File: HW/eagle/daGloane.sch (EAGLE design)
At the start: 62 parts, among them IC2 MCP1252-33X50, U1 STM32F10XTXU6

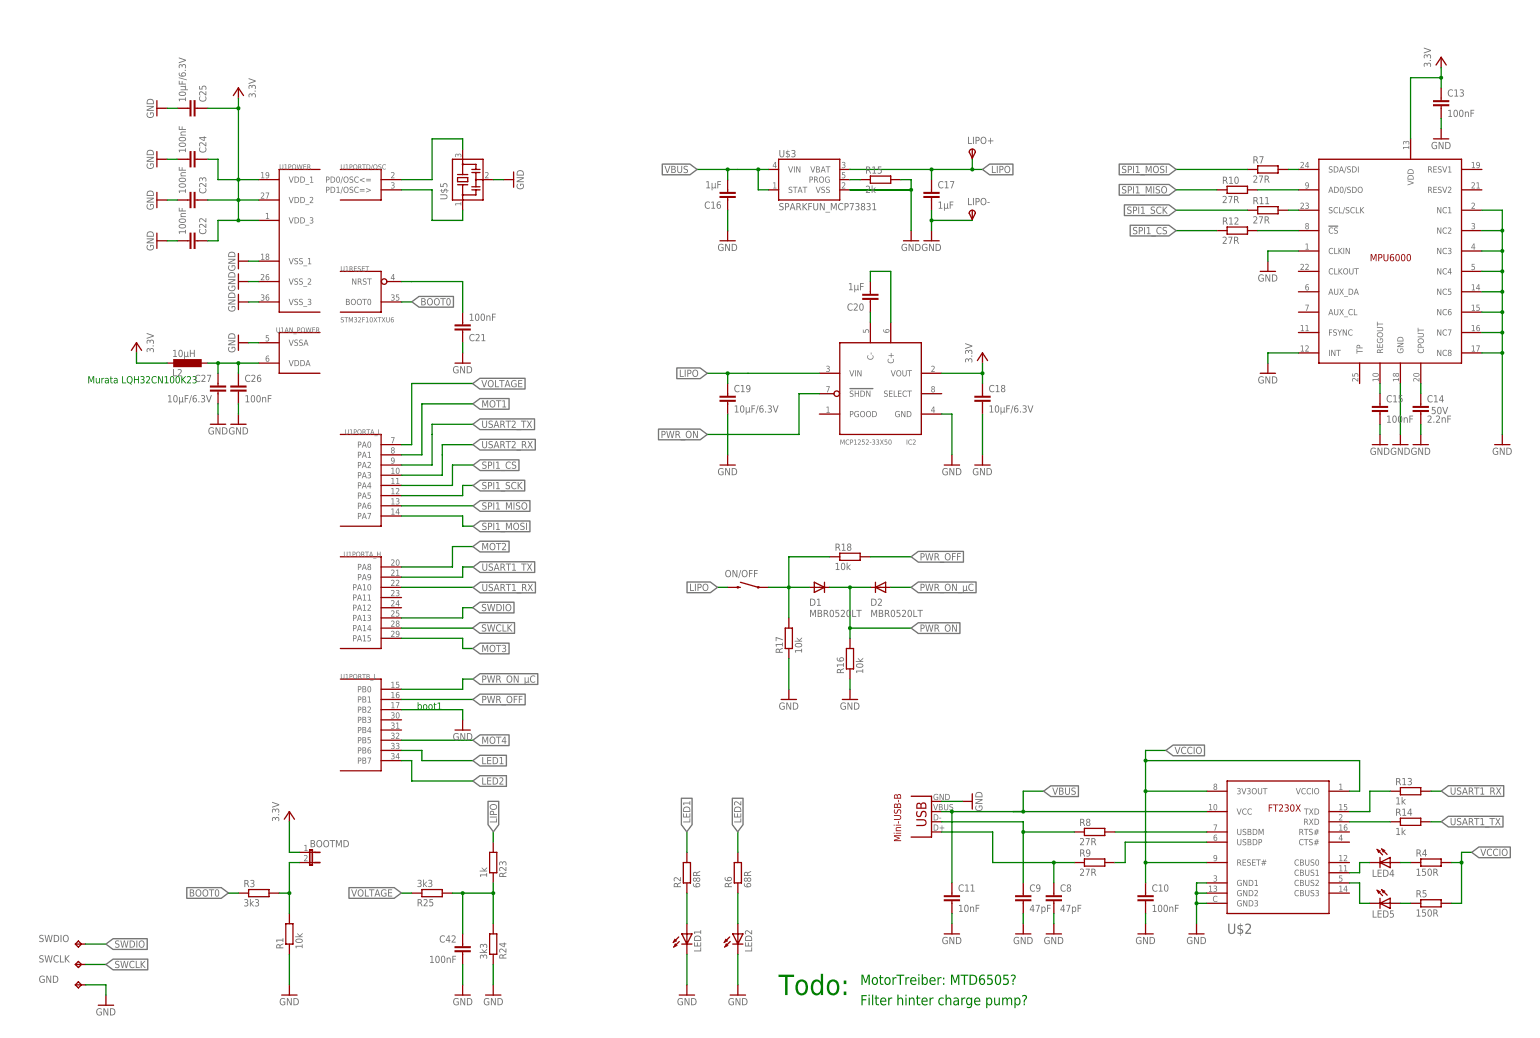
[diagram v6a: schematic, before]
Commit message: MotorPower switch added to reduce current consumption when turned off.
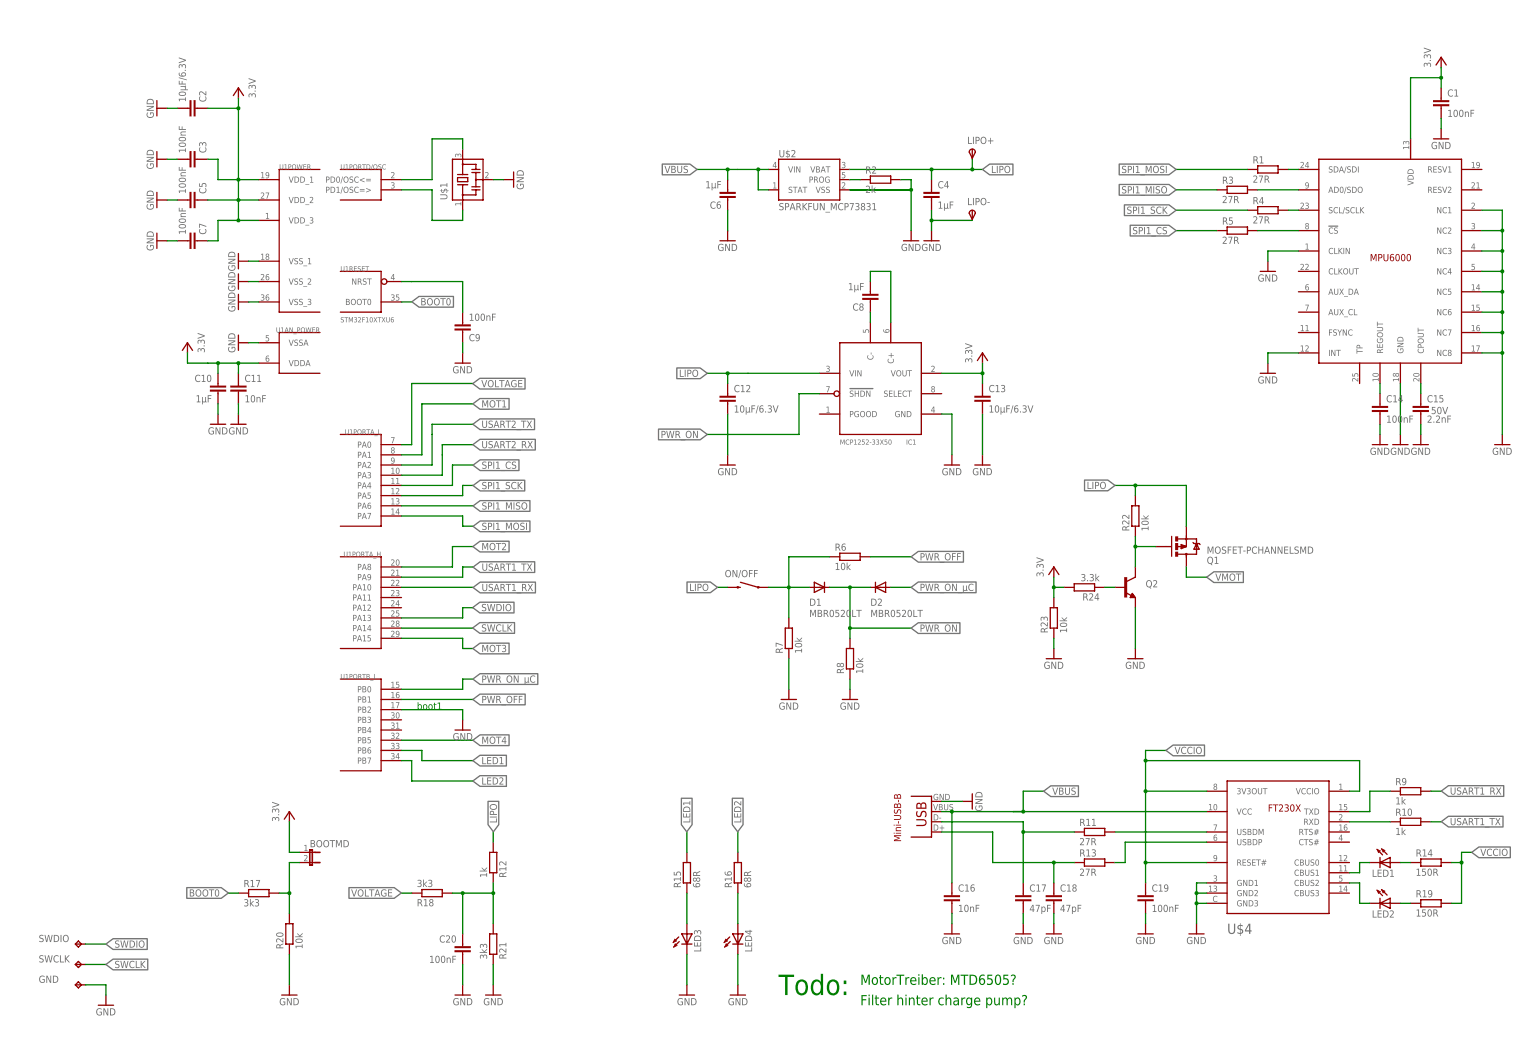
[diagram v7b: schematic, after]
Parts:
- removed C21, C26, C42: 100nF, rcl:C-EUC0603
- removed C27: 10µF/6.3V, rcl:C-EUC0805
- removed L2: 10µH, rcl:L-EUL1210
- removed LED5: (no value), led:LEDCHIPLED_0805
- removed R25: 3k3, rcl:R-EU_R0603
- removed U$5: MURATA-FILTER_CSTCE__G, canBLC2:MURATA-FILTER_CSTCE__G
- added C1: 100nF, rcl:C-EUC0603
- added C12: 10µF/6.3V, rcl:C-EUC0805
- added C4, C6: 1µF, rcl:C-EUC0603
- added LED3: (no value), led:LEDCHIPLED_0805
- added Q1: MOSFET-PCHANNELSMD, SparkFun-DiscreteSemi:MOSFET-PCHANNELSMD
- added Q2: (no value), SparkFun-DiscreteSemi:TRANSISTOR_NPNSOT23
- added R19: 150R, rcl:R-EU_R0603
- added R20, R22: 10k, rcl:R-EU_R0603
- added R21: 3k3, rcl:R-EU_R0603
- added U$4: SERIAL_FT230XQ, ftdiftx:SERIAL_FT230XQ
- C10: value 100nF -> 1µF
- C13: value 100nF -> 10µF/6.3V; device rcl:C-EUC0603 -> rcl:C-EUC0805
- C14: value 2.2nF -> 100nF; VOLTAGE 50V -> (none)
- C15: value 100nF -> 2.2nF; VOLTAGE (none) -> 50V
- C16: value 1µF -> 10nF; device rcl:C-EUC0805 -> rcl:C-EUC0603
- C17: value 1µF -> 47pF; device rcl:C-EUC0805 -> rcl:C-EUC0603
- C18: value 10µF/6.3V -> 47pF; device rcl:C-EUC0805 -> rcl:C-EUC0603
- C19: value 10µF/6.3V -> 100nF; device rcl:C-EUC0805 -> rcl:C-EUC0603
- C20: value 1µF -> 100nF; device rcl:C-EUC0805 -> rcl:C-EUC0603
- C8: value 47pF -> 1µF
- C9: value 47pF -> 100nF
- R1: value 10k -> 27R
- R10, R12, R9: value 27R -> 1k
- R13: value 1k -> 27R
- R14: value 1k -> 150R
- R15: value 2k -> 68R
- R16: value 10k -> 68R
- R17, R18: value 10k -> 3k3
- R2: value 68R -> 2k
- R23: value 1k -> 10k
- R24: value 3k3 -> 3.3k
- R3: value 3k3 -> 27R
- R4, R5: value 150R -> 27R
- R6: value 68R -> 10k
- R7, R8: value 27R -> 10k
- U$1: value MPU6000 -> MURATA-FILTER_CSTCE__G; device MPU6000:MPU6000 -> canBLC2:MURATA-FILTER_CSTCE__G
- U$2: value SERIAL_FT230XQ -> SPARKFUN_MCP73831; device ftdiftx:SERIAL_FT230XQ -> LiPo-USB-Charger-v21:SPARKFUN_MCP73831
- U$3: value SPARKFUN_MCP73831 -> MPU6000; device LiPo-USB-Charger-v21:SPARKFUN_MCP73831 -> MPU6000:MPU6000
- renumbered C22 to C7, C23 to C5, C24 to C3, C25 to C2, IC2 to IC1, USB2 to USB1
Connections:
- removed net VDDA1: C26.1, C27.1, L2.1
- new net N$26: Q2.B, R24.1
- new net N$7: Q1.G, Q2.C, R22.1
- new net VMOT: Q1.D
- net BOOT0: now also R17.1; no longer R3.1
- net D+: now also C18.1, R13.1; no longer C8.1, R9.1
- net D-: now also C17.1, R11.1; no longer C9.1, R8.1
- net GND: now also C1.2, C12.2, C16.2, C20.2, C4.2, C6.1, C9.1, LED3.C, LED4.C, Q2.E, R2.2, R20.1, R21.1, R23.1, R7.1, R8.1, U$1.2, U$2.VSS, U$3.CLKIN, U$3.GND, U$3.INT, U$3.NC1, U$3.NC2, U$3.NC3, U$3.NC4, U$3.NC5, U$3.NC6, U$3.NC7, U$3.NC8, U$4.GND1, U$4.GND2, U$4.GND3, U1AN_POWER.VSSA, U1POWER.VSS_1, U1POWER.VSS_2, U1POWER.VSS_3; no longer C16.1, C21.1, C26.2, C27.2, C42.2, C8.2, C9.2, LED1.C, LED2.C, R1.1, R15.2, R16.1, R17.1, R24.1, U$1.CLKIN, U$1.GND, U$1.INT, U$1.NC1, U$1.NC2, U$1.NC3, U$1.NC4, U$1.NC5, U$1.NC6, U$1.NC7, U$1.NC8, U$2.GND1, U$2.GND2, U$2.GND3, U$3.VSS, U$5.2
- net LED1: now also R15.2; no longer R2.2
- net LED2: now also R16.2; no longer R6.2
- net LIPO: now also C12.1, C4.1, Q1.S, R12.2, R22.2, U$2.VBAT; no longer C17.1, C19.1, R23.2, U$3.VBAT
- net N$10: now also R17.2, R20.2; no longer R1.2, R3.2
- net N$11: now also LED1.C, U$4.CBUS1; no longer LED4.C, U$2.CBUS1
- net N$12: now also LED2.C, U$4.CBUS2; no longer LED5.C, U$2.CBUS2
- net N$13: now also R4.2, U$3.SCL/SCLK; no longer R11.2, U$1.SCL/SCLK
- net N$14: now also LED1.A, R14.1; no longer LED4.A, R4.1
- net N$15: now also LED2.A, R19.1; no longer LED5.A, R5.1
- net N$16: now also R11.2, U$4.USBDM; no longer R8.2, U$2.USBDM
- net N$17: now also R13.2, U$4.USBDP; no longer R9.2, U$2.USBDP
- net N$18: now also R3.2, U$3.AD0/SDO; no longer R10.2, U$1.AD0/SDO
- net N$19: now also R1.2, U$3.SDA/SDI; no longer R7.2, U$1.SDA/SDI
- net N$2: now also U$1.3; no longer U$5.3
- net N$20: now also R9.1, U$4.TXD; no longer R13.1, U$2.TXD
- net N$21: now also R10.1, U$4.RXD; no longer R14.1, U$2.RXD
- net N$22: now also C20.1, R12.1, R18.2, R21.2; no longer C42.1, R23.1, R24.2, R25.2
- net N$23: now also R6.1, R7.2; no longer R17.2, R18.1
- net N$24: now also C8.2; no longer C20.2
- net N$25: now also U$1.1; no longer U$5.1
- net N$28: now also C8.1; no longer C20.1
- net N$3: now also R2.1, U$2.PROG; no longer R15.1, U$3.PROG
- net N$4: now also R5.2, U$3.!CS; no longer R12.2, U$1.!CS
- net N$5: now also C15.1, U$3.CPOUT; no longer C14.1, U$1.CPOUT
- net N$6: now also C14.1, U$3.REGOUT; no longer C15.1, U$1.REGOUT
- net N$8: now also LED3.A, R15.1; no longer LED1.A, R2.1
- net N$9: now also LED4.A, R16.1; no longer LED2.A, R6.1
- net PWR_OFF: now also R6.2; no longer R18.2
- net PWR_ON: now also R8.2; no longer R16.2
- net RESET1: now also C9.2; no longer C21.2
- net SPI1_CS: now also R5.1; no longer R12.1
- net SPI1_MISO: now also R3.1; no longer R10.1
- net SPI1_MOSI: now also R1.1; no longer R7.1
- net SPI1_SCK: now also R4.1; no longer R11.1
- net USART1_RX: now also R9.2; no longer R13.2
- net USART1_TX: now also R10.2; no longer R14.2
- net VBUS: now also C16.1, C6.2, U$2.STAT, U$2.VIN, U$4.VCC; no longer C11.1, C16.2, U$2.VCC, U$3.STAT, U$3.VIN
- net VCC: now also C1.1, C10.1, C11.1, R23.2, R24.2, U$3.VDD, U1AN_POWER.VDDA; no longer C18.1, L2.2, U$1.VDD
- net VCCIO: now also C19.1, R14.2, R19.2, U$4.3V3OUT, U$4.RESET#, U$4.VCCIO; no longer C10.1, R4.2, R5.2, U$2.3V3OUT, U$2.RESET#, U$2.VCCIO
- net VOLTAGE: now also R18.1; no longer R25.1
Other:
- note removed: "Murata LQH32CN100K23"
- moved on the sheet: C10, C11, C13, C14, C15, C16, C17, C18, C19, C20, C8, C9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

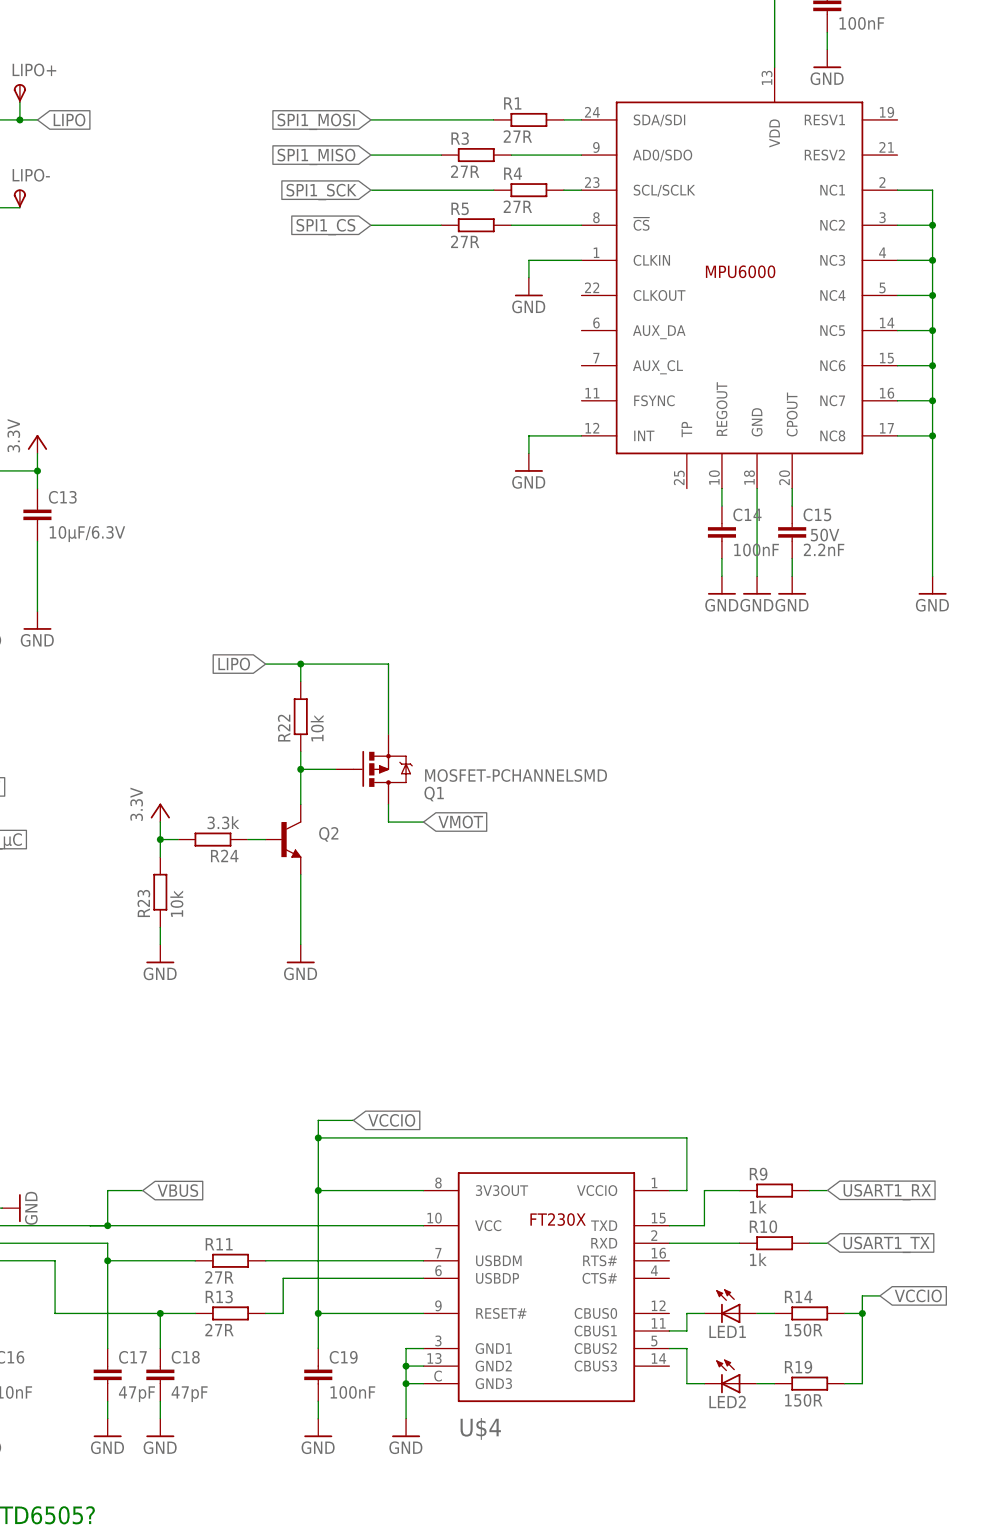
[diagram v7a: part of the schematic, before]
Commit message: package outline for MPU600 package added
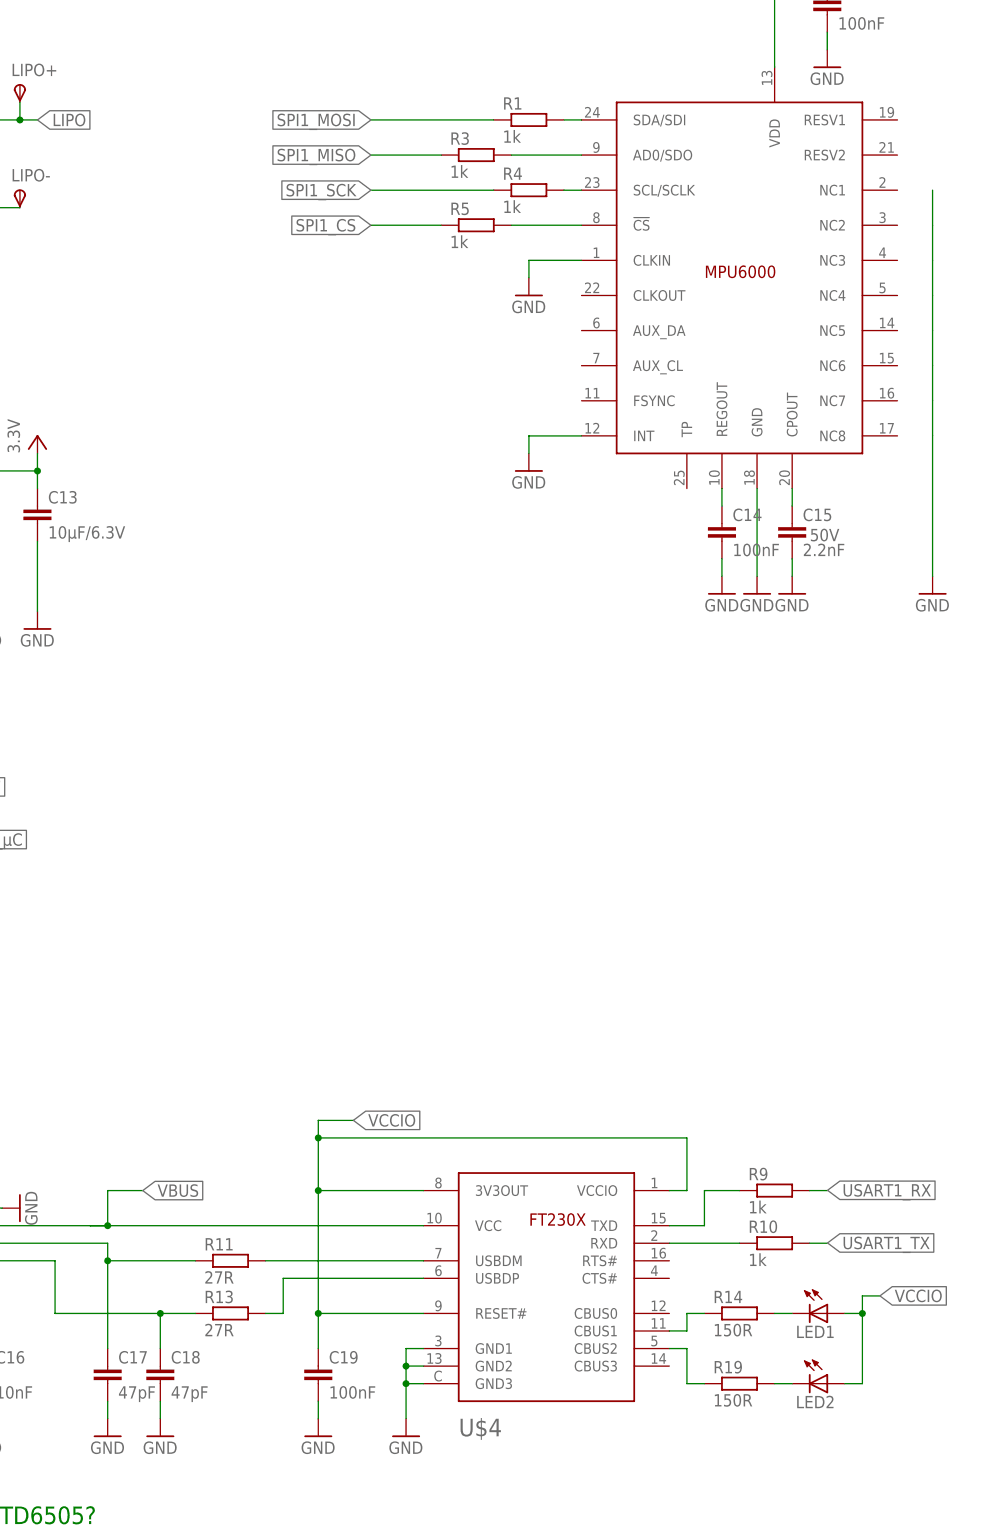
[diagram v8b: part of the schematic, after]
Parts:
- removed Q1: MOSFET-PCHANNELSMD, SparkFun-DiscreteSemi:MOSFET-PCHANNELSMD
- removed Q2: (no value), SparkFun-DiscreteSemi:TRANSISTOR_NPNSOT23
- removed R22, R23: 10k, rcl:R-EU_R0603
- removed R24: 3.3k, rcl:R-EU_R0603
- removed USB1: USB-MB-S2, con-usb:USB-MB-S2
- added X2: USB-MICROB, SparkFun-Connectors:USB-MICROB
- R1, R3, R4, R5: value 27R -> 1k
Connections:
- removed net N$15: LED2.A, R19.1
- removed net N$26: Q2.B, R24.1
- removed net N$7: Q1.G, Q2.C, R22.1
- removed net VMOT: Q1.D
- new net N$1: LED2.C, R19.2
- net D+: now also X2.D+; no longer USB1.D+
- net D-: now also X2.D-; no longer USB1.D-
- net GND: now also X2.GND; no longer Q2.E, R23.1, U$3.NC1, U$3.NC2, U$3.NC3, U$3.NC4, U$3.NC5, U$3.NC6, U$3.NC7, U$3.NC8, USB1.GND
- net LIPO: no longer Q1.S, R22.2
- net N$11: now also R14.1; no longer LED1.C
- net N$12: now also R19.1; no longer LED2.C
- net N$14: now also LED1.C, R14.2; no longer LED1.A, R14.1
- net VBUS: now also X2.VBUS; no longer USB1.VBUS
- net VCC: no longer R23.2, R24.2
- net VCCIO: now also LED1.A, LED2.A; no longer R14.2, R19.2
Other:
- moved on the sheet: LED1, LED2, R14, R19
